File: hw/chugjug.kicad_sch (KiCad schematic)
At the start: 19 parts, among them U1 STM32U575RITxQ, U2 MCP73833-xxx-UN, U3 LIS3DH, U4 MAX98357A

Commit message: sound effects working
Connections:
- net GND: now also U3.7 (SDO)
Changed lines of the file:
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@@
+	)
+	(symbol
+		(lib_id "power:GND")
+		(at 236.22 127 270)
+		(unit 1)
+		(body_style 1)
+		(exclude_from_sim no)
+		(in_bom yes)
+		(on_board yes)
+		(in_pos_files yes)
+		(dnp no)
+		(fields_autoplaced yes)
+		(property "Reference" "#PWR011"
+			(at 229.87 127 0)
+			(hide yes)
+			(show_name no)
+			(do_not_autoplace no)
+			(effects
+				(font
+					(size 1.27 1.27)
+				)
+			)
+		)
+		(property "Value" "GND"
+			(at 232.41 126.9999 90)
+			(show_name no)
+			(do_not_autoplace no)
+			(effects
+				(font
+					(size 1.27 1.27)
+				)
+				(justify right)
+			)
+		)
+		(property "Footprint" ""
+			(at 236.22 127 0)
+			(hide yes)
+			(show_name no)
+			(do_not_autoplace no)
+			(effects
+				(font
+					(size 1.27 1.27)
+				)
+			)
+		)
+		(property "Datasheet" ""
+			(at 236.22 127 0)
+			(hide yes)
+			(show_name no)
+			(do_not_autoplace no)
+			(effects
+				(font
+					(size 1.27 1.27)
+				)
+			)
+		)
+		(property "Description" "Power symbol creates a global label with name \"GND\" , ground"
+			(at 236.22 127 0)
+			(hide yes)
+			(show_name no)
+			(do_not_autoplace no)
+			(effects
+				(font
+					(size 1.27 1.27)
+				)
+			)
+		)
+		(pin "1"
+		)
+		(instances
+			(project "chugjug"
+				(path "/12a05944-430e-485f-b76a-0a82b5cd6afa"
+					(reference "#PWR011")
+					(unit 1)
+				)
+			)
+		)
 	)
 	(symbol

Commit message: hw: add 3v3 lod and stlink header
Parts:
- added J1: SAMTEC_FTSH-107-01-L-DV-K-A, chugjug:SAMTEC_FTSH-107-01-L-DV-K-A, symbol chugjug:SAMTEC_FTSH-107-01-L-DV-K-A
- added R3: 100Ω, 100R, symbol Device:R
- added U5: TPS78233DDCR, chugjug:TPS78233DDCR, symbol chugjug:TPS78233DDCR
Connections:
- net 3V3: now also J1.03
- net GND: now also U4.11 (GND), U4.15 (GND), U4.3 (GND), J1.05, J1.07, R3.1
- net I2S_BCLK: now also U4.16 (BCLK)
- net I2S_DATA: now also U4.1 (DIN)
- net I2S_LRCLK: now also U4.14 (LRCLK)
- net STLINK_NRST: now also J1.12
- net STLINK_SWCLK: now also J1.06
- net STLINK_SWDIO: now also J1.04
- net STLINK_SWO: now also J1.08
- net STLINK_UART_RX: now also J1.13
- net STLINK_UART_TX: now also J1.14
- net SD_MODE: now reaches U1.44 (PA11)
- net SD_MODE: now also U4.4 (~{SD_MODE})
- new net: J1.11, R3.2
- no-connect marks 0 -> 4
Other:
- moved on the sheet: U2

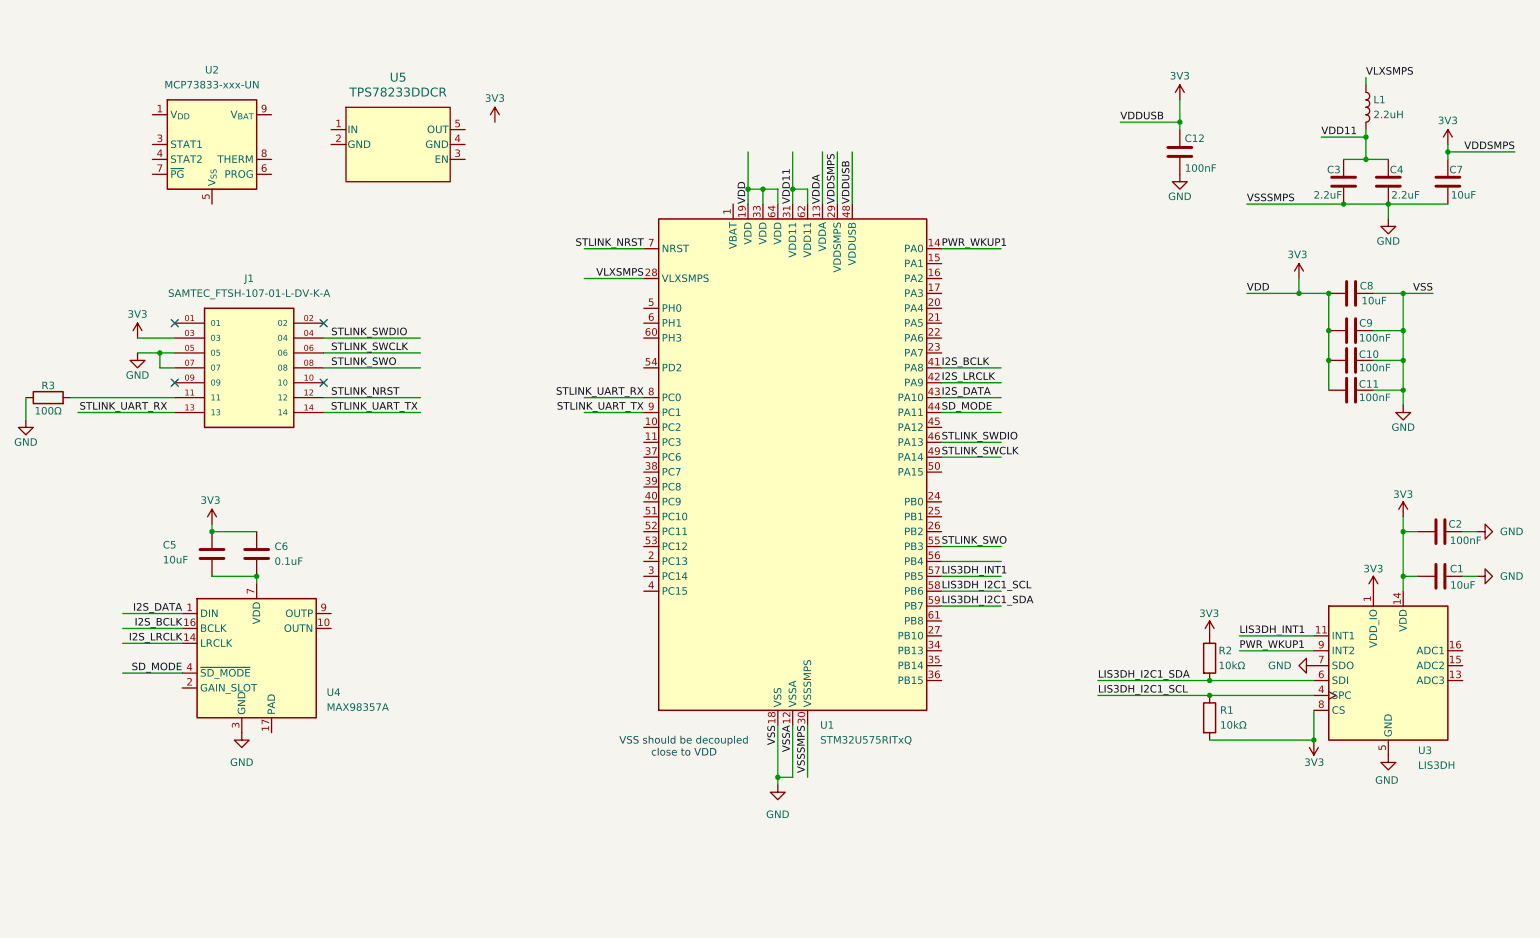
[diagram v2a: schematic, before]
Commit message: add pcb headers and ldo
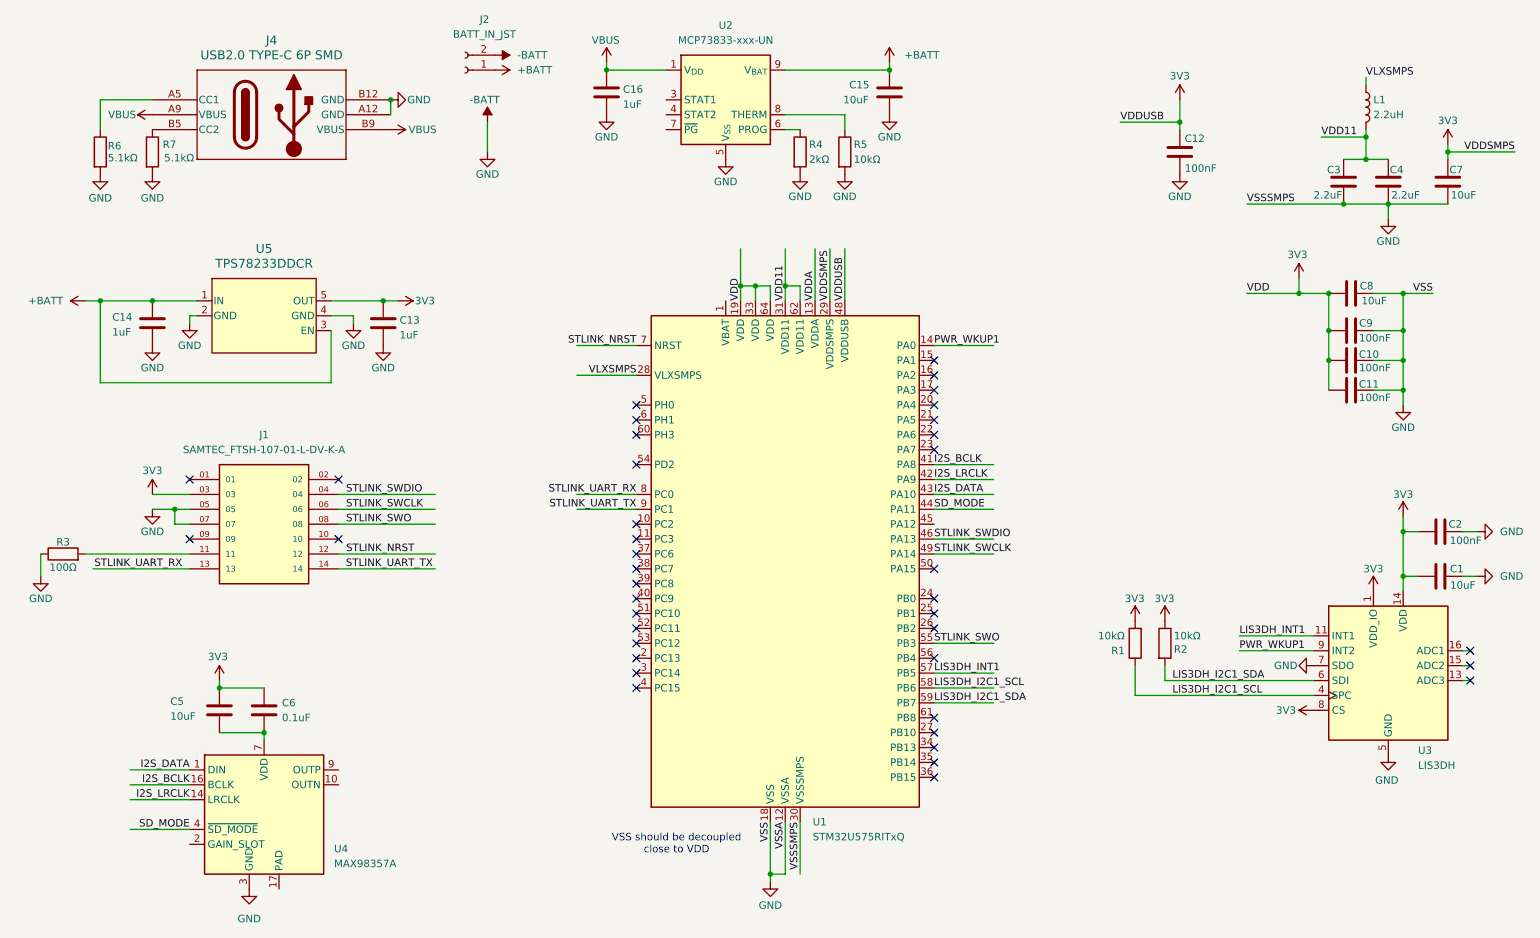
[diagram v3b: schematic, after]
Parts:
- added C13, C14, C16: 1uF, symbol Device:C
- added C15: 10uF, symbol Device:C
- added J2: BATT_IN_JST, Connector_JST:JST_PH_S2B-PH-K_1x02_P2.00mm_Horizontal, symbol Connector:Conn_01x02_Socket
- added J4: USB2.0 TYPE-C 6P SMD, chugjug:MOLEX_CONN-RCP-USB2.0-C-6POS-SMD-RA-2171750001, symbol chugjug:MOLEX_CONN-RCP-USB2.0-C-6POS-SMD-RA-2171750001
- added R4: 2kΩ, symbol Device:R
- added R5: 10kΩ, symbol Device:R
- added R6, R7: 5.1kΩ, symbol Device:R
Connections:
- net GND is gone; now on net -BATT: C1.2, C10.1, C11.1, C12.1, C2.2, C3.2, C4.2, C7.2, C8.2, C9.1, J1.05, J1.07, R3.1, U1.12 (VSSA), U1.18 (VSS), U1.30 (VSSSMPS), U1.32 (VSS), U1.47 (VSS), U1.63 (VSS), U3.10 (GND), U3.12 (GND), U3.5 (GND), U3.7 (SDO), U4.11 (GND), U4.15 (GND), U4.3 (GND)
- net 3V3: now also U5.5 (OUT), C13.1
- net VBUS: now reaches U2.1 (V_{DD}), U2.2 (V_{DD})
- net VBUS: now also C16.1, J4.A9 (VBUS), J4.B9 (VBUS)
- net +BATT: now reaches U2.10 (V_{BAT}), U2.9 (V_{BAT})
- net +BATT: now also U5.1 (IN), U5.3 (EN), C14.1, C15.1, J2.1 (Pin_1)
- net -BATT: now reaches U2.5 (V_{SS})
- net -BATT: now also U5.2 (GND), U5.4 (GND), C13.2, C14.2, C15.2, C16.2, J2.2 (Pin_2), J4.A12 (GND), J4.B12 (GND), R4.2, R5.2, R6.2, R7.2
- net at U2.6 (PROG): now also R4.1
- net at U2.8 (THERM): now also R5.1
- new net: J4.A5 (CC1), R6.1
- new net: J4.B5 (CC2), R7.1
- no-connect marks 4 -> 40
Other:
- moved on the sheet: C5, C6, J1, R1, R2, R3, U1, U2, U4, U5

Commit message: finish schematic (i think)
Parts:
- added BZ1: Buzzer, symbol Device:Buzzer
- added C17: 100nF, Capacitor_SMD:C_0402_1005Metric, symbol Device:C
- added C18: 1uF, Capacitor_SMD:C_0402_1005Metric, symbol Device:C
- added D1: LEDR, LED_SMD:LED_0603_1608Metric, symbol Device:LED
- added D2: LEDG, LED_SMD:LED_0805_2012Metric, symbol Device:LED
- added D3: LEDY, LED_SMD:LED_0805_2012Metric, symbol Device:LED
- added R10, R9: 3kΩ, Resistor_SMD:R_0402_1005Metric, symbol Device:R
- added R8: 2.2kΩ, Resistor_SMD:R_0402_1005Metric, symbol Device:R
- C1, C15, C5, C7, C8: footprint (none) -> Capacitor_SMD:C_0805_2012Metric
- C10, C11, C12, C13, C14, C16, C2, C6, C9: footprint (none) -> Capacitor_SMD:C_0402_1005Metric
- C3, C4: footprint (none) -> Capacitor_SMD:C_0603_1608Metric
- L1: footprint (none) -> Inductor_SMD:L_0805_2012Metric
- R1, R2, R4, R5, R6, R7: footprint (none) -> Resistor_SMD:R_0402_1005Metric
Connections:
- net VDDA is gone; now on net 3V3: U1.13 (VDDA)
- net -BATT: now also C17.1, C18.1
- net 3V3: now also U1.1 (VBAT), C17.2, C18.2
- net VBUS: now also D1.2 (A), D2.2 (A), D3.2 (A)
- net at C5.2, C6.2, U4.7 (VDD)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: now also U4.2 (GAIN_SLOT)
- net at U2.3 (STAT1): now also R9.2
- net at U2.4 (STAT2): now also R8.2
- net at U2.7 (~{PG}): now also R10.2
- net at U4.10 (OUTN): now also BZ1.2 (-)
- net at U4.9 (OUTP): now also BZ1.1 (+)
- new net: D3.1 (K), R9.1
- new net: D2.1 (K), R8.1
- new net: D1.1 (K), R10.1
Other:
- moved on the sheet: C1, C12, C15, C16, R4, R5, U2

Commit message: lots of layout progress
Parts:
- added D4: RLSD52A051V, Diode_SMD:D_SOD-523, symbol Diode:ESD5Zxx
- BZ1: footprint (none) -> chugjug:Buzzer_D20mm_H10mm_P10mm
- C15: value 10uF -> 1uF; footprint Capacitor_SMD:C_0805_2012Metric -> Capacitor_SMD:C_0402_1005Metric
- R3: footprint 100R -> Resistor_SMD:R_0402_1005Metric
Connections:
- net VBUS: now also D4.2 (A)
- net -BATT renamed GND
- net GND: now also D4.1 (K)
- no-connect marks 40 -> 41
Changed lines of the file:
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@@
 	)
 	(junction
+		(at 78.74 35.56)
+		(diameter 0)
+		(color 0 0 0 0)
+	)
+	(junction
 		(at 238.76 69.85)
 		(diameter 0)
@@
 	)
 	(no_connect
+		(at 171.45 102.87)
+	)
+	(no_connect
 		(at 171.45 80.01)
 	)
@@
 	(wire
 		(pts
+			(xy 78.74 35.56) (xy 78.74 38.1)
+		)
+		(stroke
+			(width 0)
+			(type default)
+		)
+	)
+	(wire
+		(pts
 			(xy 248.92 48.26) (xy 248.92 50.8)
 		)
@@
 	(wire
 		(pts
-			(xy 95.25 39.37) (xy 95.25 34.29)
-		)
-		(stroke
-			(width 0)
-			(type default)
-		)
-	)
-	(wire
-		(pts
 			(xy 224.79 48.26) (xy 248.92 48.26)
 		)
@@
 			)
 		)
-		(property "Footprint" ""
+		(property "Footprint" "chugjug:Buzzer_D20mm_H10mm_P10mm"
 			(at 74.295 143.51 90)
 			(hide yes)
@@
 	)
 	(symbol
-		(lib_id "power:-BATT")
-		(at 95.25 34.29 0)
-		(unit 1)
-		(body_style 1)
-		(exclude_from_sim no)
-		(in_bom yes)
-		(on_board yes)
-		(in_pos_files yes)
-		(dnp no)
-		(property "Reference" "#PWR033"
-			(at 95.25 38.1 0)
-			(hide yes)
-			(show_name no)
-			(do_not_autoplace no)
-			(effects
-				(font
-					(size 1.27 1.27)
-				)
-			)
-		)
-		(property "Value" "-BATT"
-			(at 92.202 30.48 0)
-			(show_name no)
-			(do_not_autoplace no)
-			(effects
-				(font
-					(size 1.27 1.27)
-				)
-				(justify left)
-			)
-		)
-		(property "Footprint" ""
-			(at 95.25 34.29 0)
-			(hide yes)
-			(show_name no)
-			(do_not_autoplace no)
-			(effects
-				(font
-					(size 1.27 1.27)
-				)
-			)
-		)
-		(property "Datasheet" ""
-			(at 95.25 34.29 0)
-			(hide yes)
-			(show_name no)
-			(do_not_autoplace no)
-			(effects
-				(font
-					(size 1.27 1.27)
-				)
-			)
-		)
-		(property "Description" "Power symbol creates a global label with name \"-BATT\""
-			(at 95.25 34.29 0)
-			(hide yes)
-			(show_name no)
-			(do_not_autoplace no)
-			(effects
-				(font
-					(size 1.27 1.27)
-				)
-			)
-		)
-		(pin "1"
-		)
-		(instances
-			(project "chugjug"
-				(path "/12a05944-430e-485f-b76a-0a82b5cd6afa"
-					(reference "#PWR033")
-					(unit 1)
-				)
-			)
-		)
-	)
-	(symbol
 		(lib_id "chugjug:MOLEX_CONN-RCP-USB2.0-C-6POS-SMD-RA-2171750001")
 		(at 58.42 33.02 0)
@@
 	)
 	(symbol
+		(lib_id "Diode:ESD5Zxx")
+		(at 78.74 41.91 90)
+		(unit 1)
+		(body_style 1)
+		(exclude_from_sim no)
+		(in_bom yes)
+		(on_board yes)
+		(in_pos_files yes)
+		(dnp no)
+		(property "Reference" "D4"
+			(at 73.914 40.64 90)
+			(show_name no)
+			(do_not_autoplace no)
+			(effects
+				(font
+					(size 1.27 1.27)
+				)
+				(justify right)
+			)
+		)
+		(property "Value" "RLSD52A051V"
+			(at 63.5 42.926 90)
+			(show_name no)
+			(do_not_autoplace no)
+			(effects
+				(font
+					(size 1.27 1.27)
+				)
+				(justify right)
+			)
+		)
+		(property "Footprint" "Diode_SMD:D_SOD-523"
+			(at 83.185 41.91 0)
+			(hide yes)
+			(show_name no)
+			(do_not_autoplace no)
+			(effects
+				(font
+					(size 1.27 1.27)
+				)
+			)
+		)
+		(property "Datasheet" ""
+			(at 78.74 41.91 0)
+			(hide yes)
+			(show_name no)
+			(do_not_autoplace no)
+			(effects
+				(font
+					(size 1.27 1.27)
+				)
+			)
+		)
+		(property "Description" "ESD Protection Diode, SOD-523"
+			(at 78.74 41.91 0)
+			(hide yes)
+			(show_name no)
+			(do_not_autoplace no)
+			(effects
+				(font
+					(size 1.27 1.27)
+				)
+			)
+		)
+		(pin "2"
+		)
+		(pin "1"
+		)
+		(instances
+			(project "chugjug"
+				(path "/12a05944-430e-485f-b76a-0a82b5cd6afa"
+					(reference "D4")
+					(unit 1)
+				)
+			)
+		)
+	)
+	(symbol
 		(lib_id "power:VDD")
 		(at 38.1 97.79 0)
@@
 	)
 	(symbol
-		(lib_id "power:-BATT")
-		(at 96.52 22.86 270)
-		(unit 1)
-		(body_style 1)
-		(exclude_from_sim no)
-		(in_bom yes)
-		(on_board yes)
-		(in_pos_files yes)
-		(dnp no)
-		(fields_autoplaced yes)
-		(property "Reference" "#PWR032"
-			(at 92.71 22.86 0)
-			(hide yes)
-			(show_name no)
-			(do_not_autoplace no)
-			(effects
-				(font
-					(size 1.27 1.27)
-				)
-			)
-		)
-		(property "Value" "-BATT"
-			(at 100.33 22.8599 90)
-			(show_name no)
-			(do_not_autoplace no)
-			(effects
-				(font
-					(size 1.27 1.27)
-				)
-				(justify left)
-			)
-		)
-		(property "Footprint" ""
-			(at 96.52 22.86 0)
-			(hide yes)
-			(show_name no)
-			(do_not_autoplace no)
-			(effects
-				(font
-					(size 1.27 1.27)
-				)
-			)
-		)
-		(property "Datasheet" ""
-			(at 96.52 22.86 0)
-			(hide yes)
-			(show_name no)
-			(do_not_autoplace no)
-			(effects
-				(font
-					(size 1.27 1.27)
-				)
-			)
-		)
-		(property "Description" "Power symbol creates a global label with name \"-BATT\""
-			(at 96.52 22.86 0)
-			(hide yes)
-			(show_name no)
-			(do_not_autoplace no)
-			(effects
-				(font
-					(size 1.27 1.27)
-				)
-			)
-		)
-		(pin "1"
-		)
-		(instances
-			(project "chugjug"
-				(path "/12a05944-430e-485f-b76a-0a82b5cd6afa"
-					(reference "#PWR032")
-					(unit 1)
-				)
-			)
-		)
-	)
-	(symbol
 		(lib_id "power:GND")
 		(at 207.01 71.12 0)
@@
 			)
 		)
-		(property "Footprint" "100R"
+		(property "Footprint" "Resistor_SMD:R_0402_1005Metric"
 			(at 22.86 109.728 90)
 			(hide yes)
@@
 			)
 		)
-		(property "Value" "10uF"
+		(property "Value" "1uF"
 			(at 177.546 30.48 0)
 			(show_name no)
@@
 			)
 		)
-		(property "Footprint" "Capacitor_SMD:C_0805_2012Metric"
+		(property "Footprint" "Capacitor_SMD:C_0402_1005Metric"
 			(at 186.3852 33.02 0)
 			(hide yes)
@@
 	)
 	(symbol
+		(lib_id "power:GND")
+		(at 78.74 45.72 0)
+		(unit 1)
+		(body_style 1)
+		(exclude_from_sim no)
+		(in_bom yes)
+		(on_board yes)
+		(in_pos_files yes)
+		(dnp no)
+		(property "Reference" "#PWR046"
+			(at 78.74 52.07 0)
+			(hide yes)
+			(show_name no)
+			(do_not_autoplace no)
+			(effects
+				(font
+					(size 1.27 1.27)
+				)
+			)
+		)
+		(property "Value" "GND"
+			(at 78.74 49.53 0)
+			(show_name no)
+			(do_not_autoplace no)
+			(effects
+				(font
+					(size 1.27 1.27)
+				)
+			)
+		)
+		(property "Footprint" ""
+			(at 78.74 45.72 0)
+			(hide yes)
+			(show_name no)
+			(do_not_autoplace no)
+			(effects
+				(font
+					(size 1.27 1.27)
+				)
+			)
+		)
+		(property "Datasheet" ""
+			(at 78.74 45.72 0)
+			(hide yes)
+			(show_name no)
+			(do_not_autoplace no)
+			(effects
+				(font
+					(size 1.27 1.27)
+				)
+			)
+		)
+		(property "Description" "Power symbol creates a global label with name \"GND\" , ground"
+			(at 78.74 45.72 0)
+			(hide yes)
+			(show_name no)
+			(do_not_autoplace no)
+			(effects
+				(font
+					(size 1.27 1.27)
+				)
+			)
+		)
+		(pin "1"
+		)
+		(instances
+			(project "chugjug"
+				(path "/12a05944-430e-485f-b76a-0a82b5cd6afa"
+					(reference "#PWR046")
+					(unit 1)
+				)
+			)
+		)
+	)
+	(symbol
 		(lib_id "Device:C")
 		(at 38.1 68.58 0)
@@
 	(symbol
 		(lib_id "power:GND")
-		(at 95.25 39.37 0)
+		(at 96.52 22.86 90)
 		(unit 1)
 		(body_style 1)
@@
 		(dnp no)
 		(property "Reference" "#PWR034"
-			(at 95.25 45.72 0)
+			(at 102.87 22.86 0)
 			(hide yes)
 			(show_name no)
@@
 		)
 		(property "Value" "GND"
-			(at 95.25 43.18 0)
+			(at 102.616 22.86 90)
 			(show_name no)
 			(do_not_autoplace no)
@@
 		)
 		(property "Footprint" ""
-			(at 95.25 39.37 0)
+			(at 96.52 22.86 0)
 			(hide yes)
 			(show_name no)
@@
 		)
 		(property "Datasheet" ""
-			(at 95.25 39.37 0)
+			(at 96.52 22.86 0)
 			(hide yes)
 			(show_name no)
@@
 		)
 		(property "Description" "Power symbol creates a global label with name \"GND\" , ground"
-			(at 95.25 39.37 0)
+			(at 96.52 22.86 0)
 			(hide yes)
 			(show_name no)

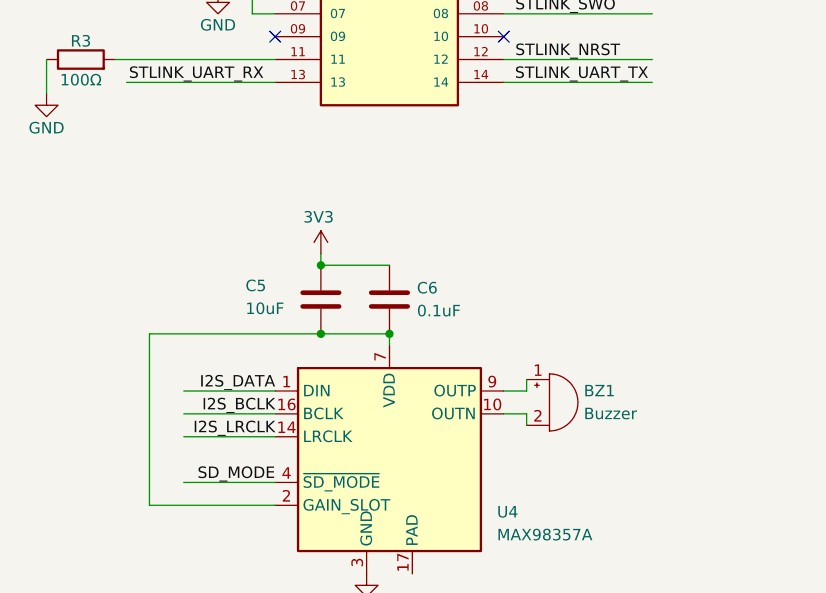
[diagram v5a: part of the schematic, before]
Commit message: much more layout changes. amp powered from +batt now
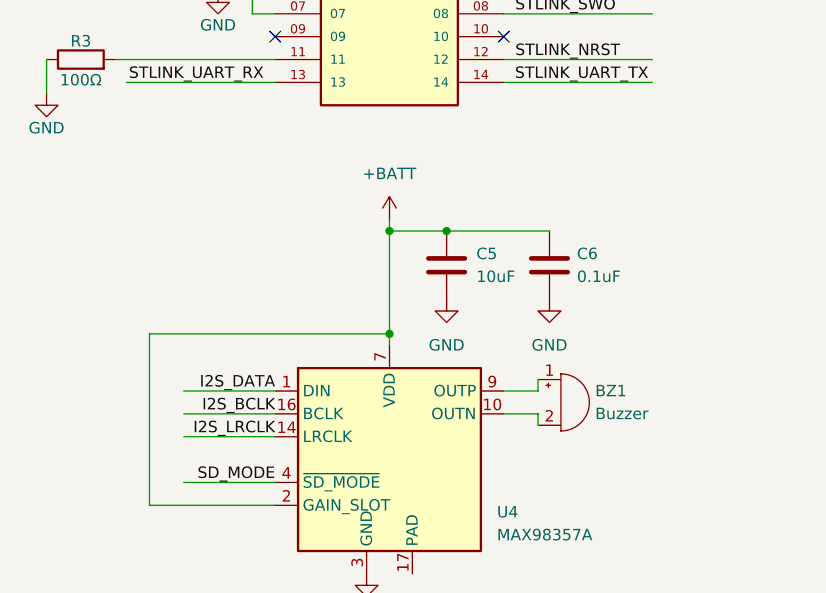
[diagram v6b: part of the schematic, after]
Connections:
- net +BATT: now also C5.1, C6.1, U4.2 (GAIN_SLOT), U4.7 (VDD), U4.8 (VDD)
- net 3V3: no longer C5.1, C6.1
- net GND: now also C5.2, C6.2
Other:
- moved on the sheet: BZ1, C5, C6

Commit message: initial layout done
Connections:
- no-connect marks 41 -> 42
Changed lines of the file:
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@@
 	)
 	(no_connect
+		(at 59.69 165.1)
+	)
+	(no_connect
 		(at 171.45 118.11)
 	)
@@
 		)
 		(property "Value" "1uF"
-			(at 177.546 30.48 0)
+			(at 178.816 30.48 0)
 			(show_name no)
 			(do_not_autoplace no)
@@
 		(pin "16"
 		)
-		(pin "17"
-		)
 		(pin "11"
 		)
@@
 		(pin "7"
 		)
+		(pin "17"
+		)
 		(instances
